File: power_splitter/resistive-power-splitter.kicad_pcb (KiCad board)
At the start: 2 copper layers, 120 x 99 mm, 0 parts

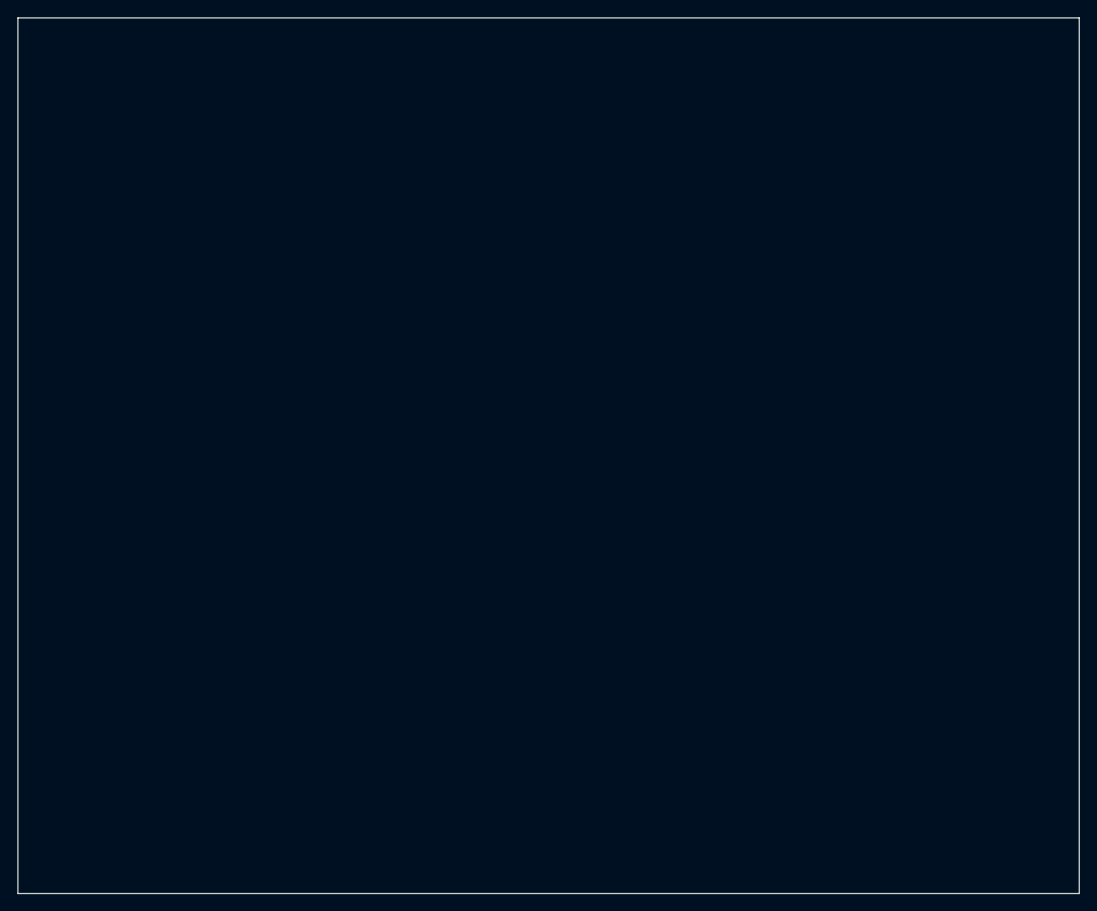
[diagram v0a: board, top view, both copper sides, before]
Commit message: power splitter: footprint assignment & parts placement
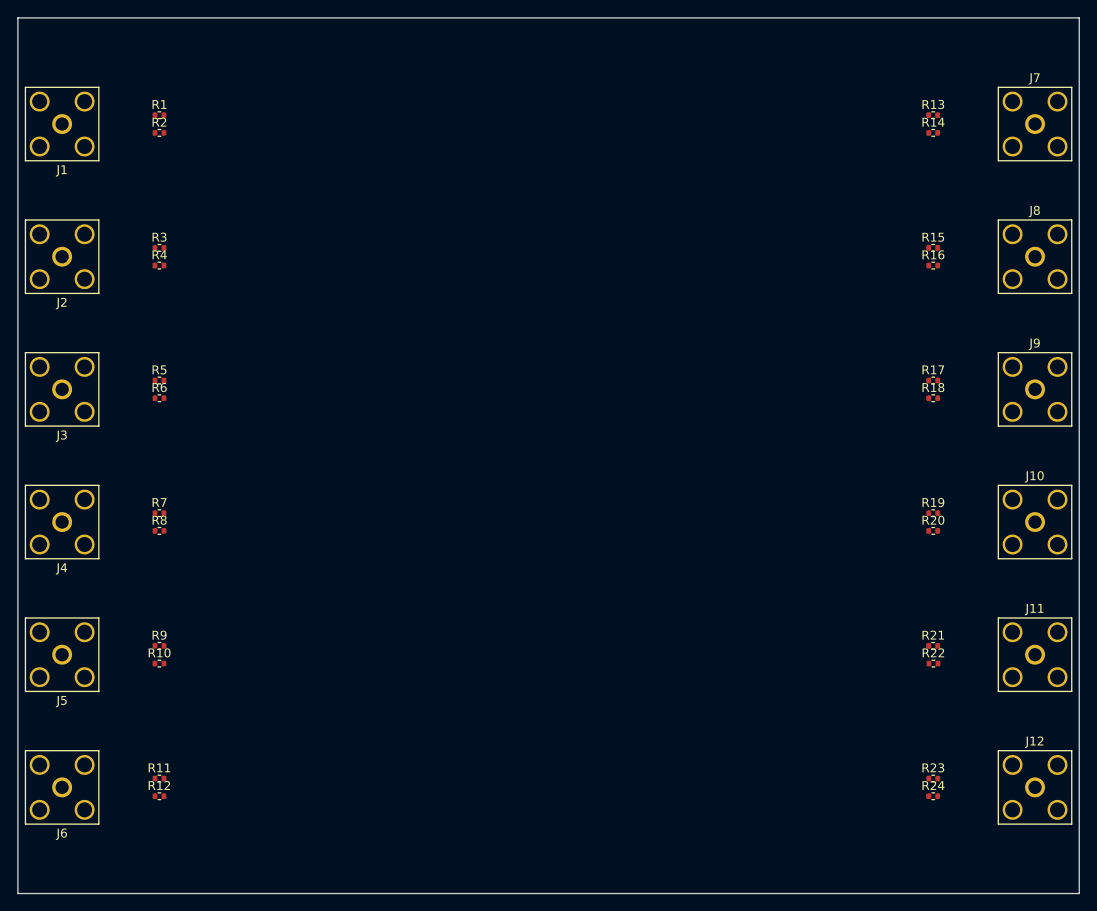
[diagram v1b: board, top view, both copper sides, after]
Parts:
- added J1: Conn_01x02, Connector_Coaxial:SMA_Amphenol_132203-12_Horizontal, F.Cu at (65.0, 63.0)
- added J10: Conn_01x02, Connector_Coaxial:SMA_Amphenol_132203-12_Horizontal, F.Cu at (175.0, 108.0)
- added J11: Conn_01x02, Connector_Coaxial:SMA_Amphenol_132203-12_Horizontal, F.Cu at (175.0, 123.0)
- added J12: Conn_01x02, Connector_Coaxial:SMA_Amphenol_132203-12_Horizontal, F.Cu at (175.0, 138.0)
- added J2: Conn_01x02, Connector_Coaxial:SMA_Amphenol_132203-12_Horizontal, F.Cu at (65.0, 78.0)
- added J3: Conn_01x02, Connector_Coaxial:SMA_Amphenol_132203-12_Horizontal, F.Cu at (65.0, 93.0)
- added J4: Conn_01x02, Connector_Coaxial:SMA_Amphenol_132203-12_Horizontal, F.Cu at (65.0, 108.0)
- added J5: Conn_01x02, Connector_Coaxial:SMA_Amphenol_132203-12_Horizontal, F.Cu at (65.0, 123.0)
- added J6: Conn_01x02, Connector_Coaxial:SMA_Amphenol_132203-12_Horizontal, F.Cu at (65.0, 138.0)
- added J7: Conn_01x02, Connector_Coaxial:SMA_Amphenol_132203-12_Horizontal, F.Cu at (175.0, 63.0)
- added J8: Conn_01x02, Connector_Coaxial:SMA_Amphenol_132203-12_Horizontal, F.Cu at (175.0, 78.0)
- added J9: Conn_01x02, Connector_Coaxial:SMA_Amphenol_132203-12_Horizontal, F.Cu at (175.0, 93.0)
- added R1: 82, Resistor_SMD:R_0402_1005Metric, F.Cu at (76.0, 62.0)
- added R10: 82, Resistor_SMD:R_0402_1005Metric, F.Cu at (76.0, 124.0)
- added R11: 82, Resistor_SMD:R_0402_1005Metric, F.Cu at (76.0, 137.0)
- added R12: 82, Resistor_SMD:R_0402_1005Metric, F.Cu at (76.0, 139.0)
- added R13: 82, Resistor_SMD:R_0402_1005Metric, F.Cu at (163.5, 62.0)
- added R14: 82, Resistor_SMD:R_0402_1005Metric, F.Cu at (163.5, 64.0)
- added R15: 82, Resistor_SMD:R_0402_1005Metric, F.Cu at (163.5, 77.0)
- added R16: 82, Resistor_SMD:R_0402_1005Metric, F.Cu at (163.5, 79.0)
- added R17: 82, Resistor_SMD:R_0402_1005Metric, F.Cu at (163.5, 92.0)
- added R18: 82, Resistor_SMD:R_0402_1005Metric, F.Cu at (163.5, 94.0)
- added R19: 82, Resistor_SMD:R_0402_1005Metric, F.Cu at (163.5, 107.0)
- added R2: 82, Resistor_SMD:R_0402_1005Metric, F.Cu at (76.0, 64.0)
- added R20: 82, Resistor_SMD:R_0402_1005Metric, F.Cu at (163.5, 109.0)
- added R21: 82, Resistor_SMD:R_0402_1005Metric, F.Cu at (163.5, 122.0)
- added R22: 82, Resistor_SMD:R_0402_1005Metric, F.Cu at (163.5, 124.0)
- added R23: 82, Resistor_SMD:R_0402_1005Metric, F.Cu at (163.5, 137.0)
- added R24: 82, Resistor_SMD:R_0402_1005Metric, F.Cu at (163.5, 139.0)
- added R3: 82, Resistor_SMD:R_0402_1005Metric, F.Cu at (76.0, 77.0)
- added R4: 82, Resistor_SMD:R_0402_1005Metric, F.Cu at (76.0, 79.0)
- added R5: 82, Resistor_SMD:R_0402_1005Metric, F.Cu at (76.0, 92.0)
- added R6: 82, Resistor_SMD:R_0402_1005Metric, F.Cu at (76.0, 94.0)
- added R7: 82, Resistor_SMD:R_0402_1005Metric, F.Cu at (76.0, 107.0)
- added R8: 82, Resistor_SMD:R_0402_1005Metric, F.Cu at (76.0, 109.0)
- added R9: 82, Resistor_SMD:R_0402_1005Metric, F.Cu at (76.0, 122.0)

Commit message: power splitter: PCB routing, fill zones and solder masks
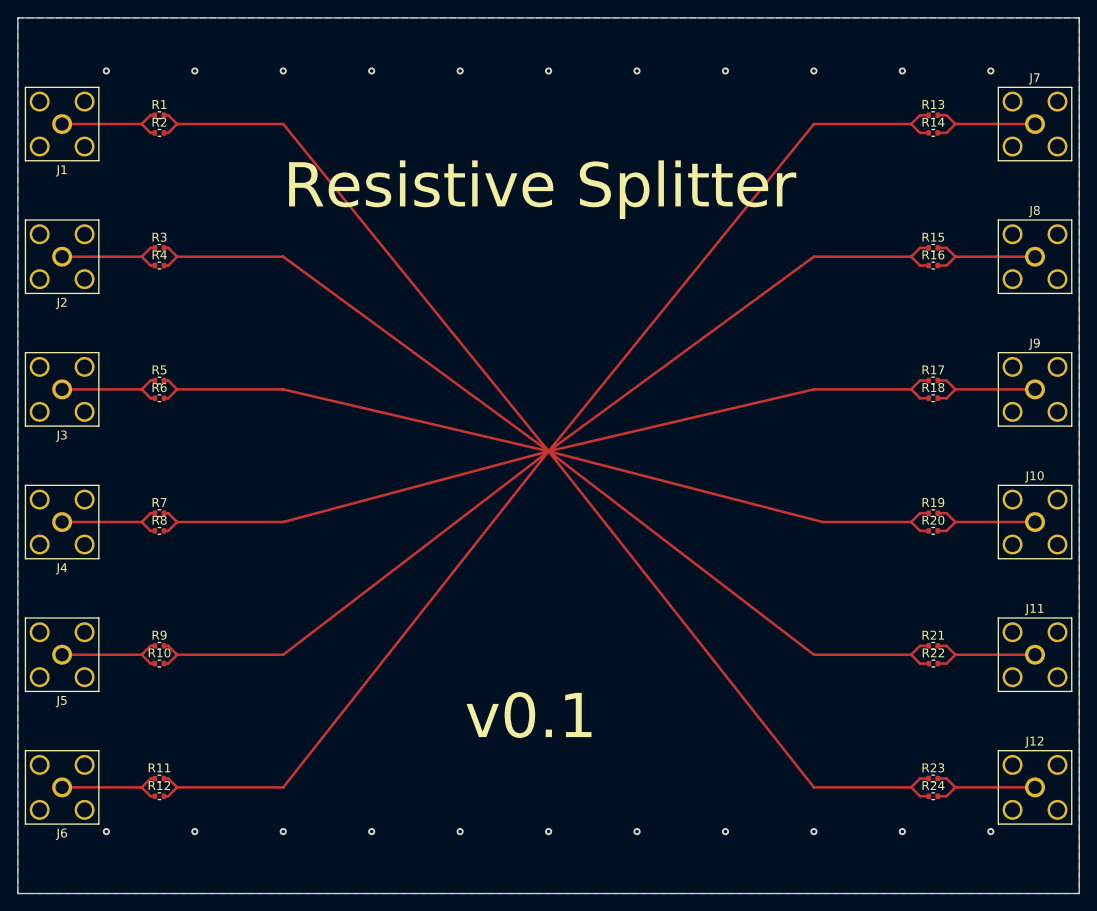
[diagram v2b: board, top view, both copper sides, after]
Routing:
- net Net-(R1-Pad2): track 0.00 -> 655.4 mm
- net Net-(J9-Pad1): track 0.00 -> 13.8 mm
- net Net-(J8-Pad1): track 0.00 -> 13.8 mm
- net Net-(J7-Pad1): track 0.00 -> 13.8 mm
- net Net-(J12-Pad1): track 0.00 -> 13.8 mm
- net Net-(J10-Pad1): track 0.00 -> 13.8 mm
- net Net-(J11-Pad1): track 0.00 -> 13.8 mm
- net Net-(J6-Pad1): track 0.00 -> 12.8 mm
- net Net-(J5-Pad1): track 0.00 -> 12.8 mm
- net Net-(J4-Pad1): track 0.00 -> 12.8 mm
- net Net-(J3-Pad1): track 0.00 -> 12.8 mm
- net Net-(J2-Pad1): track 0.00 -> 12.8 mm
- net Net-(J1-Pad1): track 0.00 -> 12.8 mm
- net GND: vias 0 -> 22
- added copper zone on B.Cu, net GND
- added copper zone on In1.Cu, net GND
- added copper zone on In2.Cu, net GND
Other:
- copper layers 2 -> 4
- board text added: "Resistive Splitter"
- board text added: "v0.1"

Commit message: power splitter: add front layer copper fills on border
This is intentionally with a solder mask, so that the PCB will be
connected to the casing.
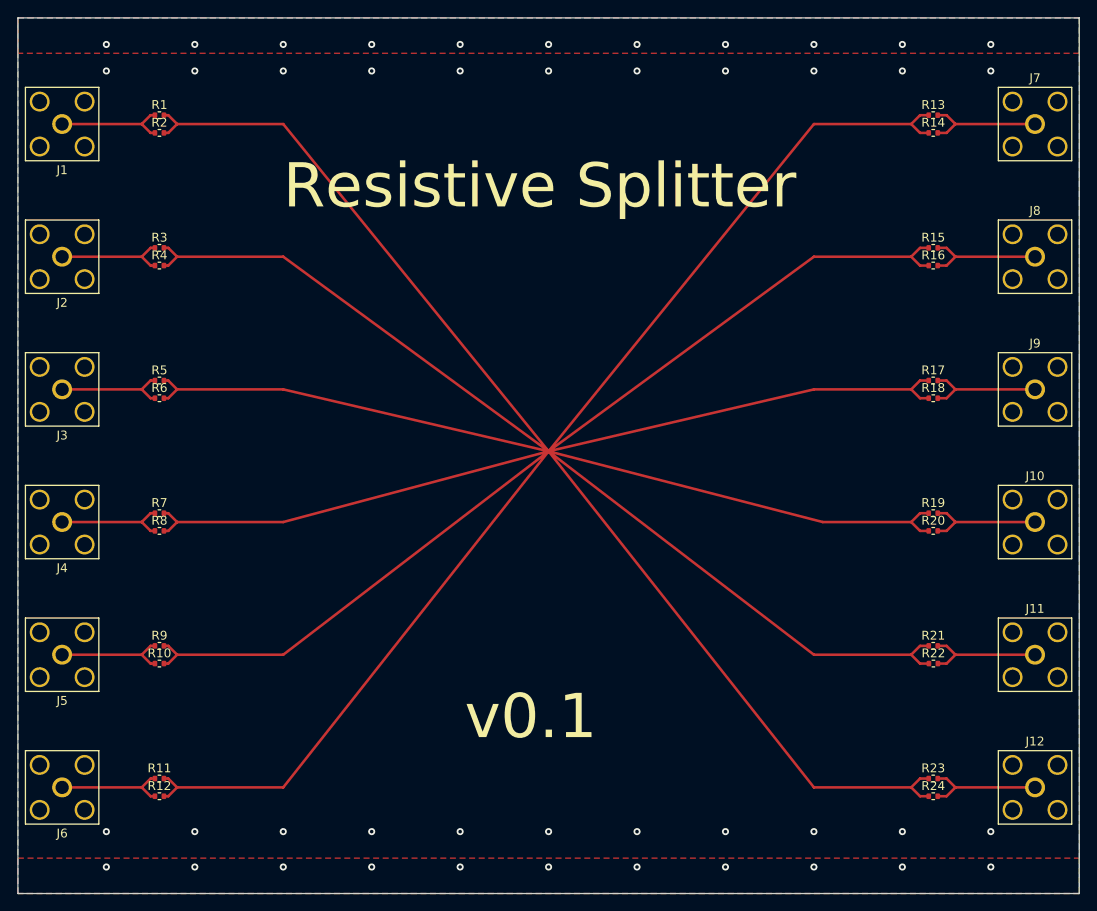
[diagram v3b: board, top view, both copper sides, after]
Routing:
- net GND: vias 22 -> 44
- added copper zone on F.Cu, net GND
